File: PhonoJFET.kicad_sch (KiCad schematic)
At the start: 38 parts, among them J1 Conn_01x02, J2 Conn_01x03, J3 Barrel_Jack_Switch, J4 Conn_01x02, J5 Conn_01x03, J6 Conn_01x01, J7 Conn_01x01, J8 Conn_01x01, J9 Conn_01x01, U1 TL072

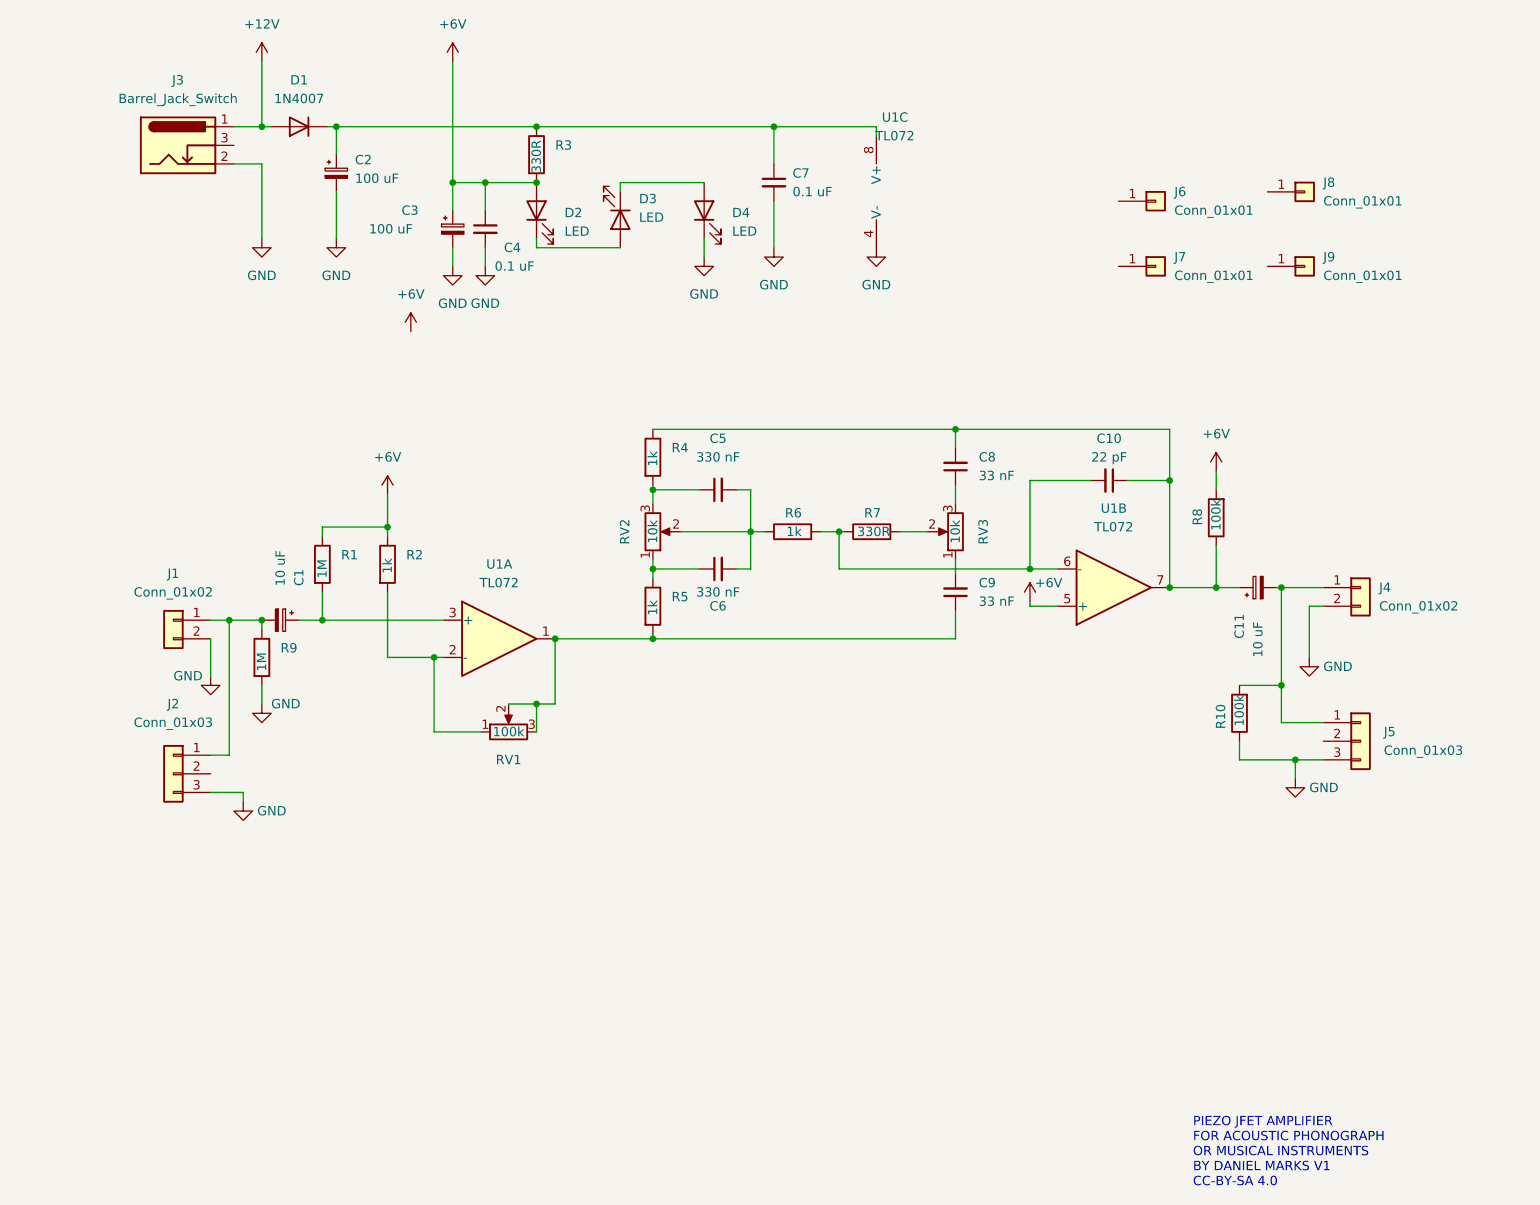
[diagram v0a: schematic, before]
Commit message: Fixed some component values and biases
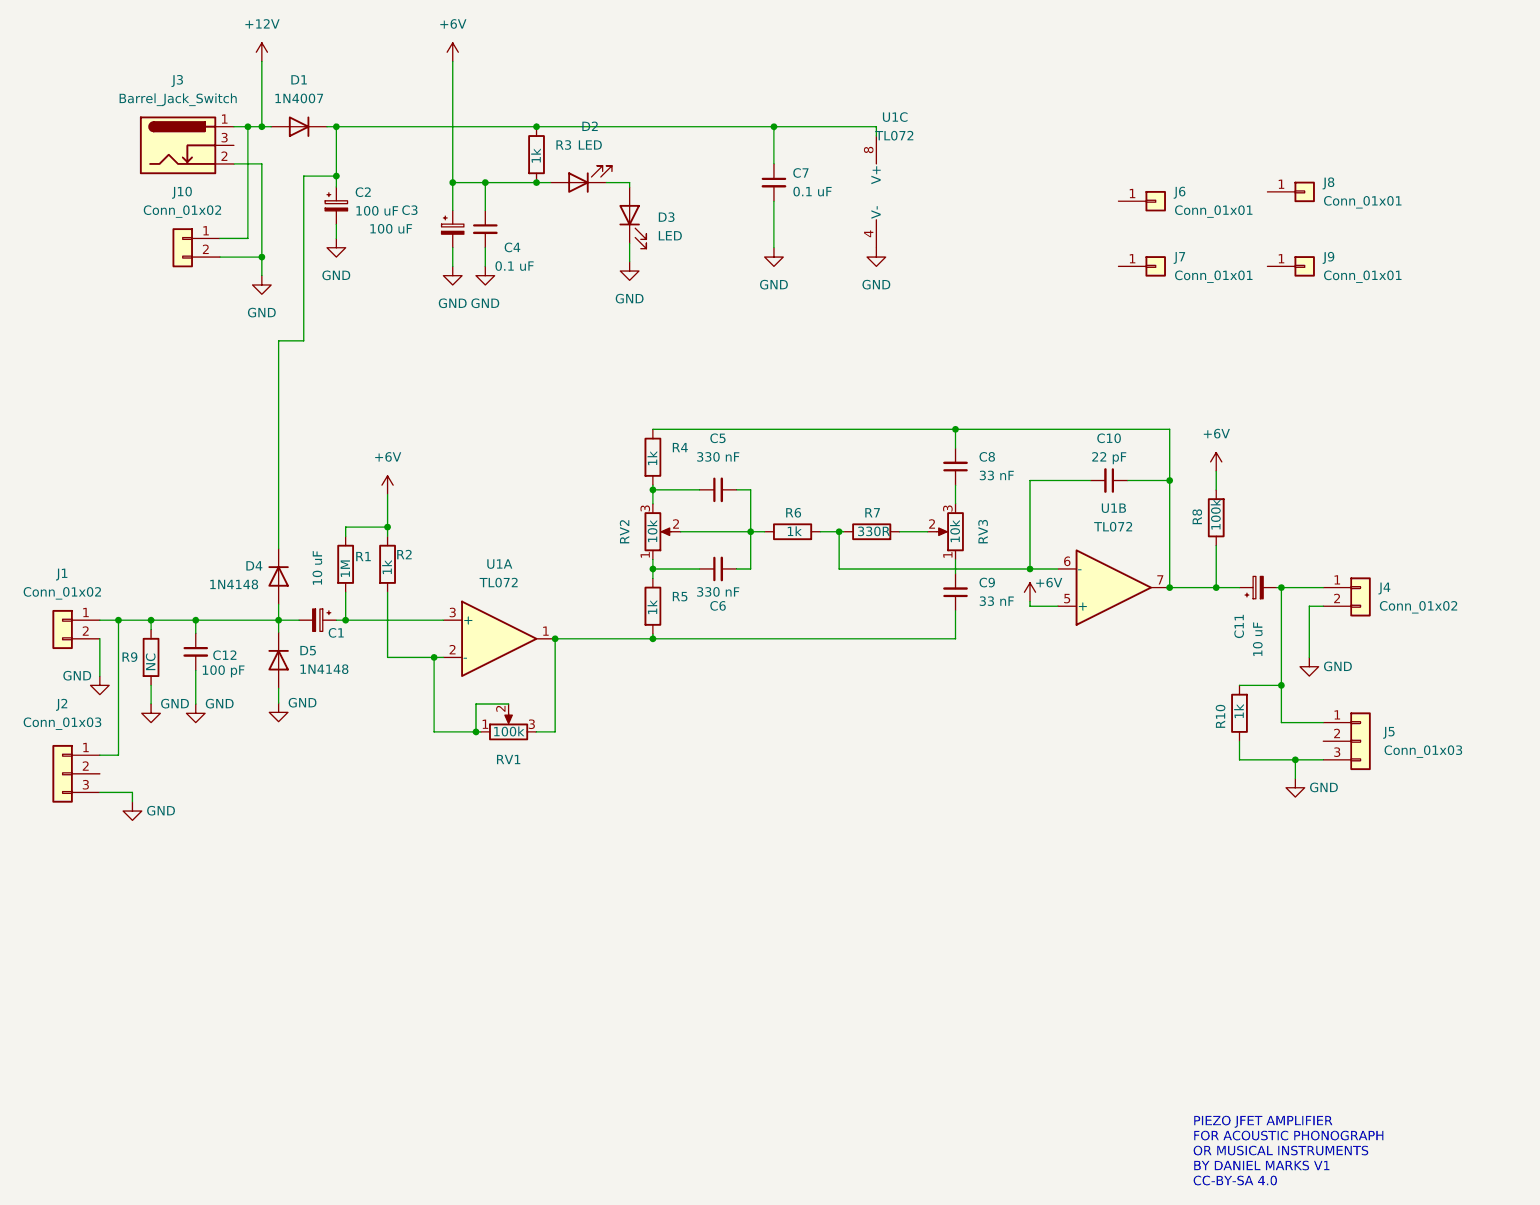
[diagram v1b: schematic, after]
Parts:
- removed D4: LED, LED_THT:LED_D3.0mm, symbol Device:LED
- added C12: 100 pF, Capacitor_THT:C_Disc_D5.0mm_W2.5mm_P5.00mm, symbol Device:C_Small
- added D4, D5: 1N4148, Diode_THT:D_DO-41_SOD81_P7.62mm_Horizontal, symbol Device:D
- added J10: Conn_01x02, TerminalBlock:TerminalBlock_bornier-2_P5.08mm, symbol Connector_Generic:Conn_01x02
- R10: value 100k -> 1k
- R3: value 330R -> 1k
- R9: value 1M -> NC
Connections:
- net +12V: now also J10.1 (Pin_1)
- net GND: now also D3.1 (K), C12.2, D5.2 (A), J10.2 (Pin_2)
- net at C2.1, C7.1, D1.1 (K)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: now also D4.1 (K)
- net at C1.2, J1.1 (Pin_1), J2.1 (Pin_1)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: now also C12.1, D4.2 (A), D5.1 (K)
- net at C9.1, R5.2, RV1.3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: no longer RV1.2
- net at R2.2, RV1.1, U1.2 (-): now also RV1.2
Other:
- moved on the sheet: C1, C2, D2, D3, J1, J2, R1, R9

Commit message: Modified pcb
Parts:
- added R11: 100R, Resistor_THT:R_Axial_DIN0207_L6.3mm_D2.5mm_P7.62mm_Horizontal, symbol Device:R
- R2: value 1k -> 100R
- RV1: value 100k -> 10k
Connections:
- net at J4.1 (Pin_1), J5.1 (Pin_1), R10.2: now also R11.2; no longer C11.2
- new net: C11.2, R11.1
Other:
- moved on the sheet: C11, J4, J5
